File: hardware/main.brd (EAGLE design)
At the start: 60.9 x 38.1 mm, 35 parts, among them IC1 LM358D, T3 IRF840

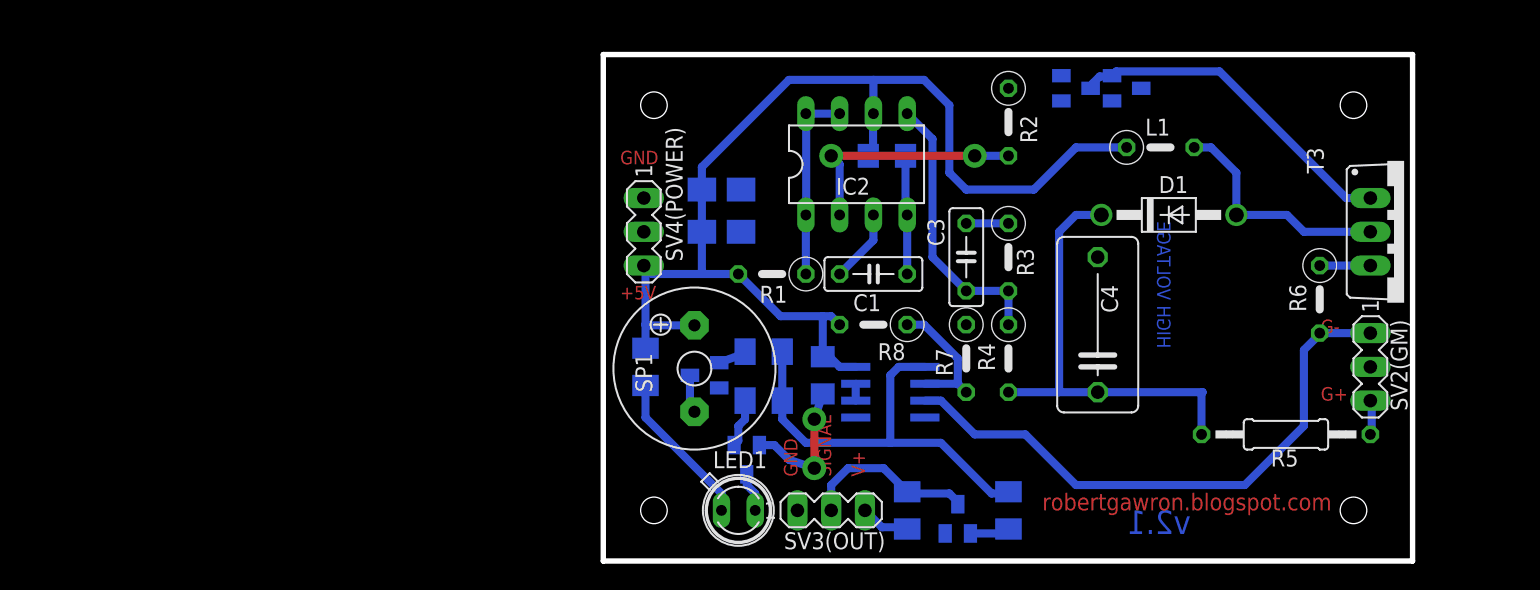
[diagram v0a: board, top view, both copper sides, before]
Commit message: Folder structure changed.
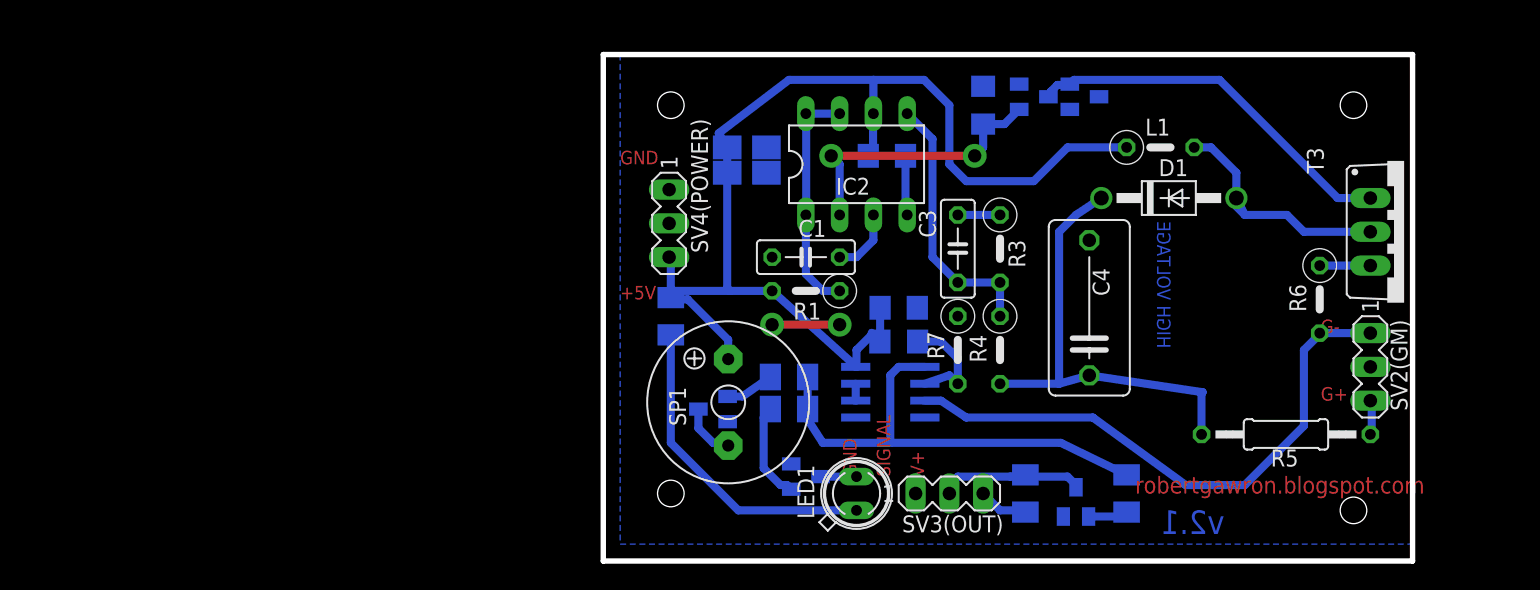
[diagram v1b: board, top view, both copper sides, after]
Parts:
- C1: value 322 -> 32n
- C3: value 102 -> 10n
- IC2: value (none) -> MC34063
- R1: value (none) -> R22/0.5W
- R2, R8: device resistor:0207/5V -> resistor:R1206
- moved R13 8.98 mm to (74.9, 5.08)
- moved R9 8.98 mm to (82.5, 5.08)
- moved SV3(OUT) 8.98 mm to (69.2, 5.08)
- moved T7 8.98 mm to (78.7, 4.45)
- moved LED1 8.98 mm to (62.2, 5.08), turned to 90 degrees
- moved C5 7.65 mm to (65.4, 19.1), turned to 180 degrees
- moved C1 5.24 mm to (58.4, 22.9), turned to 180 degrees
- moved C7 4.84 mm to (54.0, 29.2)
- moved T6 4.62 mm to (58.4, 6.35), turned to 90 degrees
- moved R12 4.26 mm to (48.3, 18.4)
- moved C6 3.70 mm to (54.0, 31.1)
- moved SP1 3.59 mm to (52.6, 11.9)
- moved D2 3.24 mm to (75.6, 34.9)
- moved T1 3.24 mm to (79.4, 34.9)
- moved R1 2.84 mm to (58.4, 20.3)
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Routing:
- net N$6: track 11.8 -> 24.2 mm
- net V-: track 26.3 -> 16.6 mm
- net N$2: track 3.68 -> 7.39 mm
- net N$14: track 18.0 -> 21.3 mm
- net N$11: track 14.6 -> 17.7 mm
- net N$16: track 25.7 -> 28.7 mm
- net N$8: track 34.1 -> 36.8 mm
- net N$4: track 13.3 -> 11.0 mm
- net N$19: track 10.1 -> 8.30 mm
- net N$10: track 2.14 -> 3.67 mm
- net V+: track 89.3 -> 90.8 mm
- net N$9: track 2.88 -> 4.22 mm
- net N$13: track 20.9 -> 20.0 mm
- net N$17: track 44.3 -> 43.7 mm
- net N$12: track 33.6 -> 34.1 mm
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
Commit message: PCB is now fixed.
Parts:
- removed IC1: LM358D, linear:SO08
- removed SV2(GM), SV3(OUT), SV4(POWER): (no value), con-lstb:MA03-1
- removed T2, T6, T7: (no value), transistor-npn:SOT23
- removed T3: IRF840, transistor-power:TO220BV
- added IC3: MC34063AD, mc34063:SOIC8
- added J1, J2: 22-05-7028-02, con-molex:7395-02
- added JP1: (no value), jumper:JP1
- added Q1: IRF840, transistor-power:TO220BV
- added Q2, Q3, Q4: (no value), transistor-npn:SOT23
- added R14: (no value), resistor:M0805
- added SV2: (no value), con-lstb:MA03-1
- C1: device resistor:C050-025X075 -> resistor:C0805
- C2: value 100n -> 32n; device resistor:C3216 -> resistor:C0805
- C3: value 10n -> 100n; device resistor:C050-025X075 -> resistor:C0805
- C4: value 100n/630V -> 10n; device resistor:C102-064X133 -> resistor:C0805
- C5: value 100n -> 100n/630V; device resistor:C3216 -> resistor:C102-064X133
- C6: value 330u -> 100n; device resistor:A/3216-18W -> resistor:C0805
- C7: device resistor:A/3216-18W -> rcl:D/7343-31R
- D1: value 1n4007 -> BAS40; device diode:DO41-10 -> diode:SOT23
- D2: value BAS40 -> 1n4007; device diode:SOT23 -> diode:DO41-10
- IC2: value MC34063 -> LM358D; device ic-package:DIL08 -> linear:SO08
- R1: value R22/0.5W -> 10k; device resistor:0207/5V -> resistor:R0805
- R10, R11: device resistor:M1206 -> resistor:M0805
- R12: value 510R -> 1k; device resistor:M1206 -> resistor:M0805
- R13: value (none) -> 510R; device resistor:M1206 -> resistor:M0805
- R2: value 10k -> R22/0.5W; device resistor:R1206 -> resistor:0207/5V
- R3: value 30k+1k -> 10M
- R4: value 10M -> 30k+1k; device resistor:0207/5V -> resistor:R0805
- R5: value 6M8 -> 30k+1k; device resistor:0207/12 -> resistor:R0805
- R6: value 10k -> 6M8
- R7: value 470R -> 10k
- R8: device resistor:R1206 -> resistor:R0805
- R9: value 1k -> 470R; device resistor:M1206 -> resistor:R0805
- moved R5 69.9 mm to (26.0, 23.5), flipped to the bottom, turned to 90 degrees
- moved R9 66.1 mm to (17.8, 18.4)
- moved R13 64.1 mm to (10.8, 4.45), turned to 0 degrees
- moved C4 59.0 mm to (21.0, 23.5), flipped to the bottom
- moved R6 55.9 mm to (41.2, 17.1)
- moved R2 53.3 mm to (18.4, 34.3), flipped to the top, turned to 0 degrees
- moved C2 53.1 mm to (11.4, 31.1), turned to 0 degrees
- moved D1 52.8 mm to (33.7, 36.2), flipped to the bottom, turned to 90 degrees
- moved IC2 51.0 mm to (14.0, 13.3), flipped to the bottom, turned to 270 degrees
- moved L1 50.8 mm to (34.3, 31.8)
- moved R8 50.8 mm to (14.6, 17.1)
- moved R3 50.6 mm to (22.9, 17.1)
- moved R4 50.1 mm to (23.5, 23.5), flipped to the bottom
- moved C1 48.2 mm to (11.4, 33.7), flipped to the bottom, turned to 0 degrees
- moved C3 47.3 mm to (23.2, 31.8), flipped to the bottom
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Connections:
- removed net N$20: R5.2, SV2(GM).3
- new net N$18: J2.1, R6.2
- new net N$7: IC3.1, IC3.7, IC3.8, L1.1, R2.1
- net N$1: now also Q4.1, R12.2; no longer R9.2, T7.1
- net N$10: now also Q2.1, R10.2; no longer R11.2, T2.1
- net N$11: now also R4.1, R5.2; no longer IC2.1, IC2.7, IC2.8, R1.1
- net N$12: now also C5.1, D2.C, R3.2, R6.1; no longer C4.1, D1.C, R4.2, R5.1
- net N$13: now also C4.1, IC3.5, R3.1, R4.2; no longer C3.1, IC2.5, R3.2, R4.1
- net N$14: now also D1.1, IC3.2, R1.2; no longer D2.1, IC2.2, R2.2
- net N$15: now also D2.A, Q1.D; no longer D1.A, T3.D
- net N$16: now also D1.3, Q1.G; no longer D2.3, T3.G
- net N$17: now also IC2.3, J2.2, R7.2; no longer IC1.3, R6.2, SV2(GM).1
- net N$19: now also IC2.2, R9.2; no longer IC1.2, R7.2
- net N$2: now also Q3.1, R11.2; no longer R10.2, T6.1
- net N$21: now also JP1.2, R14.2, SV2.3; no longer R13.2, SV3(OUT).3
- net N$22: now also IC2.6, IC2.7; no longer IC1.6, IC1.7
- net N$3: now also Q3.3; no longer T6.3
- net N$4: now also Q4.3, R14.1, SV2.2; no longer R13.1, SV3(OUT).2, T7.3
- net N$5: now also C2.1, IC3.3; no longer IC2.3
- net N$6: now also R13.1; no longer R12.1
- net N$8: now also IC2.1, R12.1; no longer IC1.1, R9.1
- net N$9: now also Q2.3; no longer T2.3
- net V+: now also C3.1, C6.1, IC2.8, IC3.6, J1.1, JP1.1, R13.2, R2.2; no longer C2.1, C5.1, C6.+, IC1.8, IC2.6, L1.1, R1.2, R12.2, SV4(POWER).3
- net V-: now also C6.2, IC2.5, IC3.4, J1.2, Q1.S, Q2.2, Q3.2, Q4.2, R1.1, R5.1, R9.1, SV2.1; no longer C6.-, IC1.4, IC1.5, R2.1, R3.1, R6.1, SV3(OUT).1, SV4(POWER).1, T2.2, T3.S, T6.2, T7.2
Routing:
- net N$7: track 0.00 -> 36.8 mm, vias 0 -> 2
- net N$8: track 36.8 -> 14.0 mm
- net V+: track 90.8 -> 113.1 mm
- net N$6: track 24.2 -> 2.23 mm
- net N$11: track 17.7 -> 2.54 mm
- net N$12: track 34.1 -> 21.6 mm
- net N$17: track 43.7 -> 33.1 mm
- net N$14: track 21.3 -> 30.2 mm
- net N$16: track 28.7 -> 20.6 mm
- net N$18: track 0.00 -> 5.13 mm
- net N$2: track 7.39 -> 2.51 mm
- net N$4: track 11.0 -> 6.34 mm
- net V-: track 16.6 -> 20.3 mm
- net N$21: track 3.75 -> 7.12 mm
- net N$15: track 18.2 -> 15.1 mm
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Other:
- board size 60.9 x 38.1 mm -> 50 x 40 mm
- board text added: "+5V DC"
- board text added: "POWER"
- board text added: "V+ is Vcc"
- board text added: "rev2.2"
- board text removed: "+5V"
- board text removed: "v2.1"
